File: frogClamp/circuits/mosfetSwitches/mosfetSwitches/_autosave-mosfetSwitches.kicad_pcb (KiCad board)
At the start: 2 copper layers, 26 x 22 mm, 7 parts, among them J1 Conn_01x05_Pin, Q1 IRLR8726, Q2 IRLR8726

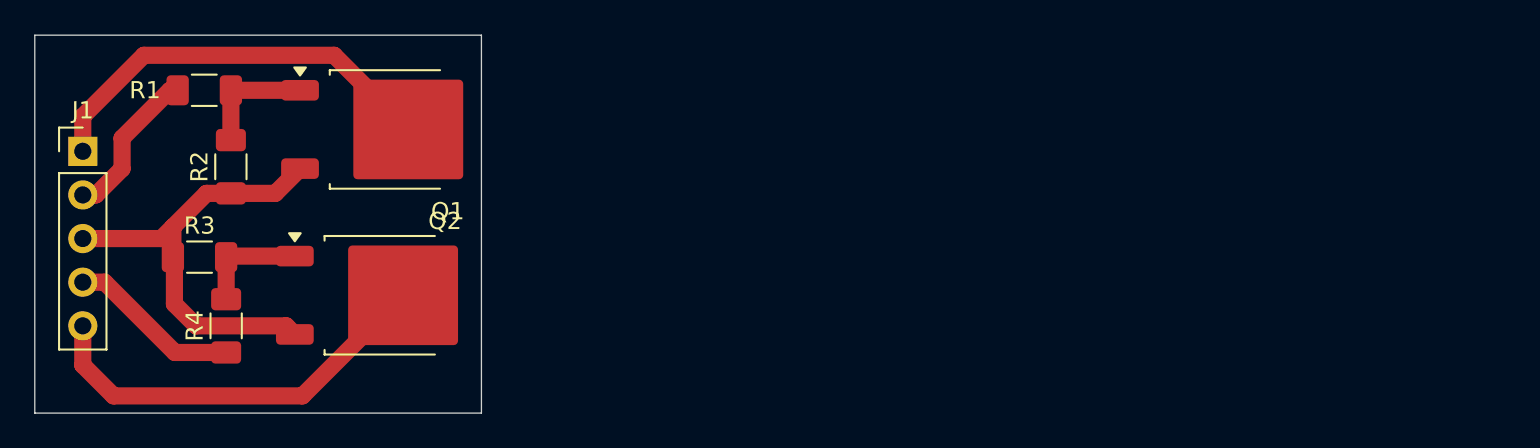
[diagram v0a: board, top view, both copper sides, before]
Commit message: Running gcode full programs in buffered method. Needs testing.
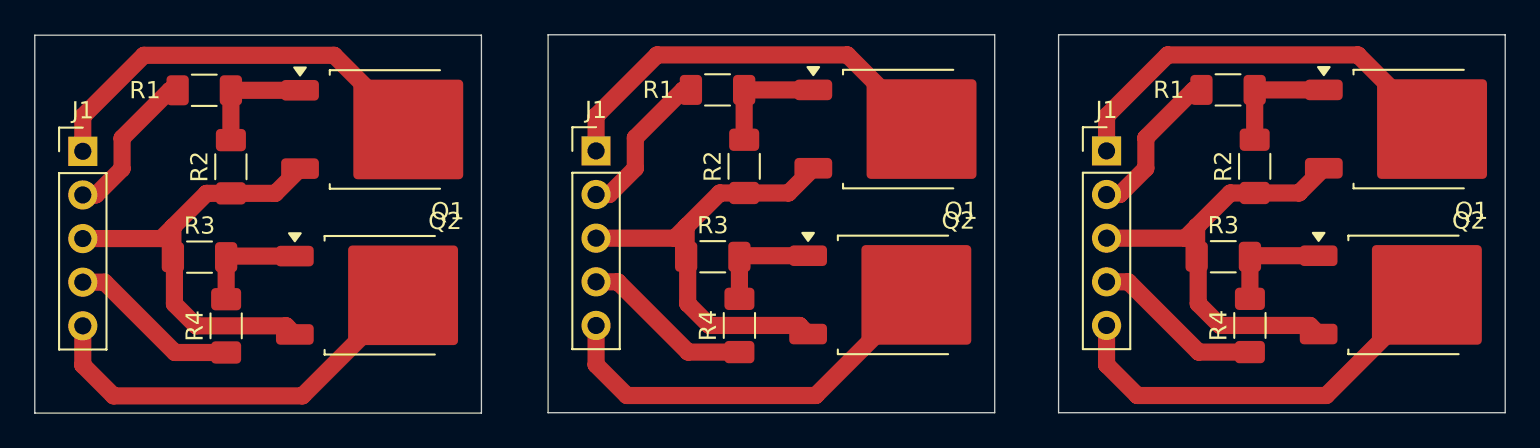
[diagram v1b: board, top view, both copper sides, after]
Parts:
- added J1: Conn_01x05_Pin, Connector_PinHeader_2.54mm:PinHeader_1x05_P2.54mm_Vertical, F.Cu at (169.7, 84.7)
- added J1: Conn_01x05_Pin, Connector_PinHeader_2.54mm:PinHeader_1x05_P2.54mm_Vertical, F.Cu at (199.4, 84.7)
- added Q1: IRLR8726, Package_TO_SOT_SMD:TO-252-2, F.Cu at (217.1, 83.5)
- added Q1: IRLR8726, Package_TO_SOT_SMD:TO-252-2, F.Cu at (187.4, 83.5)
- added Q2: IRLR8726, Package_TO_SOT_SMD:TO-252-2, F.Cu at (187.1, 93.1)
- added Q2: IRLR8726, Package_TO_SOT_SMD:TO-252-2, F.Cu at (216.8, 93.1)
- added R1: R, Resistor_SMD:R_1206_3216Metric_Pad1.30x1.75mm_HandSolder, F.Cu at (206.5, 81.2)
- added R1: R, Resistor_SMD:R_1206_3216Metric_Pad1.30x1.75mm_HandSolder, F.Cu at (176.7, 81.2)
- added R2: R, Resistor_SMD:R_1206_3216Metric_Pad1.30x1.75mm_HandSolder, F.Cu at (208.0, 85.6)
- added R2: R, Resistor_SMD:R_1206_3216Metric_Pad1.30x1.75mm_HandSolder, F.Cu at (178.3, 85.6)
- added R3: R, Resistor_SMD:R_1206_3216Metric_Pad1.30x1.75mm_HandSolder, F.Cu at (176.5, 90.9)
- added R3: R, Resistor_SMD:R_1206_3216Metric_Pad1.30x1.75mm_HandSolder, F.Cu at (206.2, 90.9)
- added R4: R, Resistor_SMD:R_1206_3216Metric_Pad1.30x1.75mm_HandSolder, F.Cu at (207.7, 94.9)
- added R4: R, Resistor_SMD:R_1206_3216Metric_Pad1.30x1.75mm_HandSolder, F.Cu at (178.0, 94.9)
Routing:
- net GND: track 26.6 -> 79.8 mm
- net /MOT1: track 24.2 -> 72.7 mm
- net /MOT2: track 24.1 -> 72.3 mm
- net /IN2: track 10.0 -> 30.1 mm
- net /IN1: track 9.09 -> 27.3 mm
- net Net-(Q1-G): track 6.92 -> 20.8 mm
- net Net-(Q2-G): track 6.47 -> 19.4 mm
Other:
- board size 26 x 22 mm -> 85.6 x 22 mm

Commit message: Added svg debug
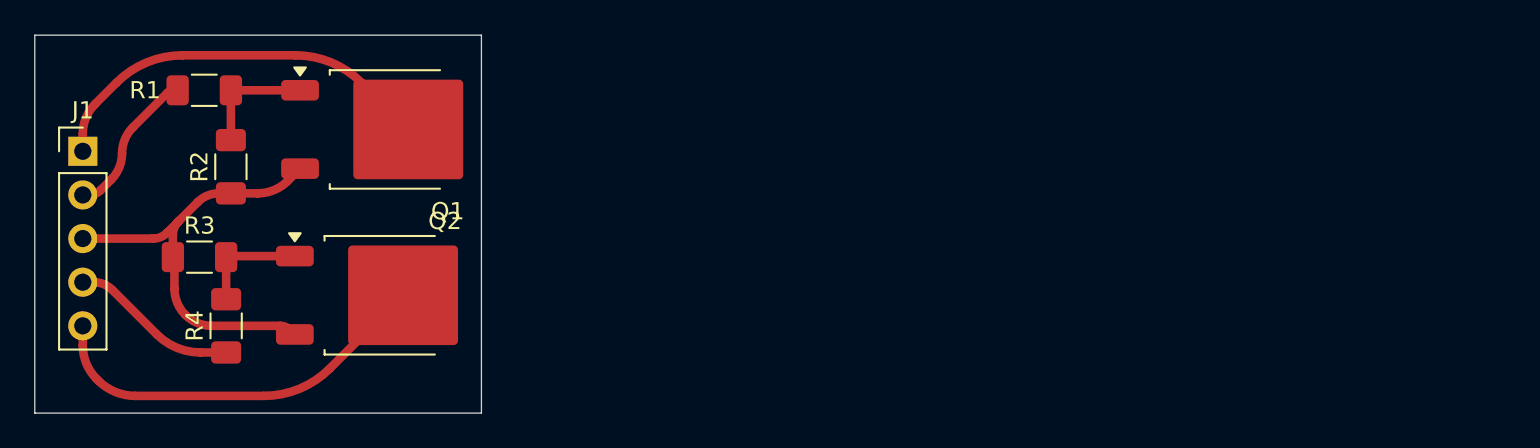
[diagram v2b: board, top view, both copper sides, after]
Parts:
- removed the J1 at (169.7, 84.7)
- removed the J1 at (199.4, 84.7)
- removed the Q1 at (217.1, 83.5)
- removed the Q1 at (187.4, 83.5)
- removed the Q2 at (187.1, 93.1)
- removed the Q2 at (216.8, 93.1)
- removed the R1 at (206.5, 81.2)
- removed the R1 at (176.7, 81.2)
- removed the R2 at (208.0, 85.6)
- removed the R2 at (178.3, 85.6)
- removed the R3 at (176.5, 90.9)
- removed the R3 at (206.2, 90.9)
- removed the R4 at (207.7, 94.9)
- removed the R4 at (178.0, 94.9)
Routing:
- net GND: track 79.8 -> 26.9 mm
- net /MOT1: track 72.7 -> 23.6 mm
- net /MOT2: track 72.3 -> 23.6 mm
- net /IN2: track 30.1 -> 9.79 mm
- net /IN1: track 27.3 -> 8.81 mm
- net Net-(Q1-G): track 20.8 -> 6.92 mm
- net Net-(Q2-G): track 19.4 -> 6.47 mm
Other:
- board size 85.6 x 22 mm -> 26 x 22 mm
